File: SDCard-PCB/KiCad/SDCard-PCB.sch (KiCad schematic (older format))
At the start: 0 parts

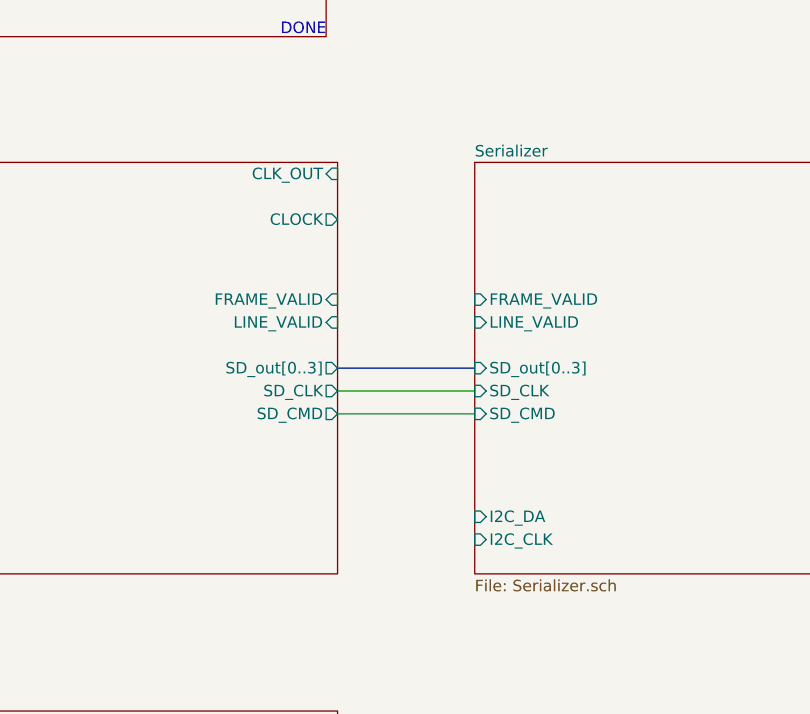
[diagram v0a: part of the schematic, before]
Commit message: Finish schematics, begin PCB design
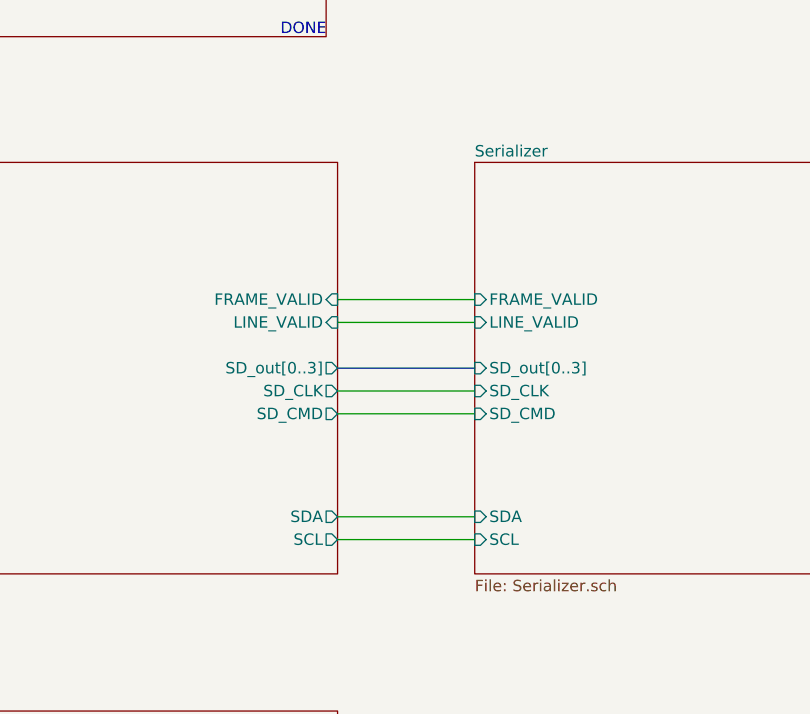
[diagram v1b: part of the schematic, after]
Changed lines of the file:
@@
 F3 "LINE_VALID" I L 7600 4150 50
 F4 "SD_out[0..3]" I L 7600 4350 50
-F5 "I2C_DA" I L 7600 5000 50
-F6 "I2C_CLK" I L 7600 5100 50
-F7 "SD_CMD" I L 7600 4550 50
-F8 "SD_CLK" I L 7600 4450 50
+F5 "SD_CMD" I L 7600 4550 50
+F6 "SD_CLK" I L 7600 4450 50
+F7 "SDA" I L 7600 5000 50
+F8 "SCL" I L 7600 5100 50
 $EndSheet
 Wire Wire Line
@@
 F4 "SD_out[0..3]" O R 7000 4350 50
 F5 "LINE_VALID" I R 7000 4150 50
-F6 "CLK_OUT" I R 7000 3500 50
-F7 "CLOCK" O R 7000 3700 50
-F8 "FRAME_VALID" I R 7000 4050 50
-F9 "SD_in[0..3]" I L 4150 3650 50
-F10 "SD_inCLK" I L 4150 3850 50
-F11 "SD_inCMD" I L 4150 3950 50
-F12 "SD_CLK" O R 7000 4450 50
-F13 "SD_CMD" O R 7000 4550 50
+F6 "FRAME_VALID" I R 7000 4050 50
+F7 "SD_in[0..3]" I L 4150 3650 50
+F8 "SD_inCLK" I L 4150 3850 50
+F9 "SD_inCMD" I L 4150 3950 50
+F10 "SD_CLK" O R 7000 4450 50
+F11 "SD_CMD" O R 7000 4550 50
+F12 "SDA" O R 7000 5000 50
+F13 "SCL" O R 7000 5100 50
 $EndSheet
 Wire Bus Line
@@
 Wire Wire Line
 	7000 4550 7600 4550
+Wire Wire Line
+	7000 4050 7600 4050
+Wire Wire Line
+	7000 4150 7600 4150
+Wire Wire Line
+	7000 5000 7600 5000
+Wire Wire Line
+	7000 5100 7600 5100
 $EndSCHEMATC
